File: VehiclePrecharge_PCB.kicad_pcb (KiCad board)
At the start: 4 copper layers, 75 x 90 mm, 12 parts, among them K1 2-1904058-5

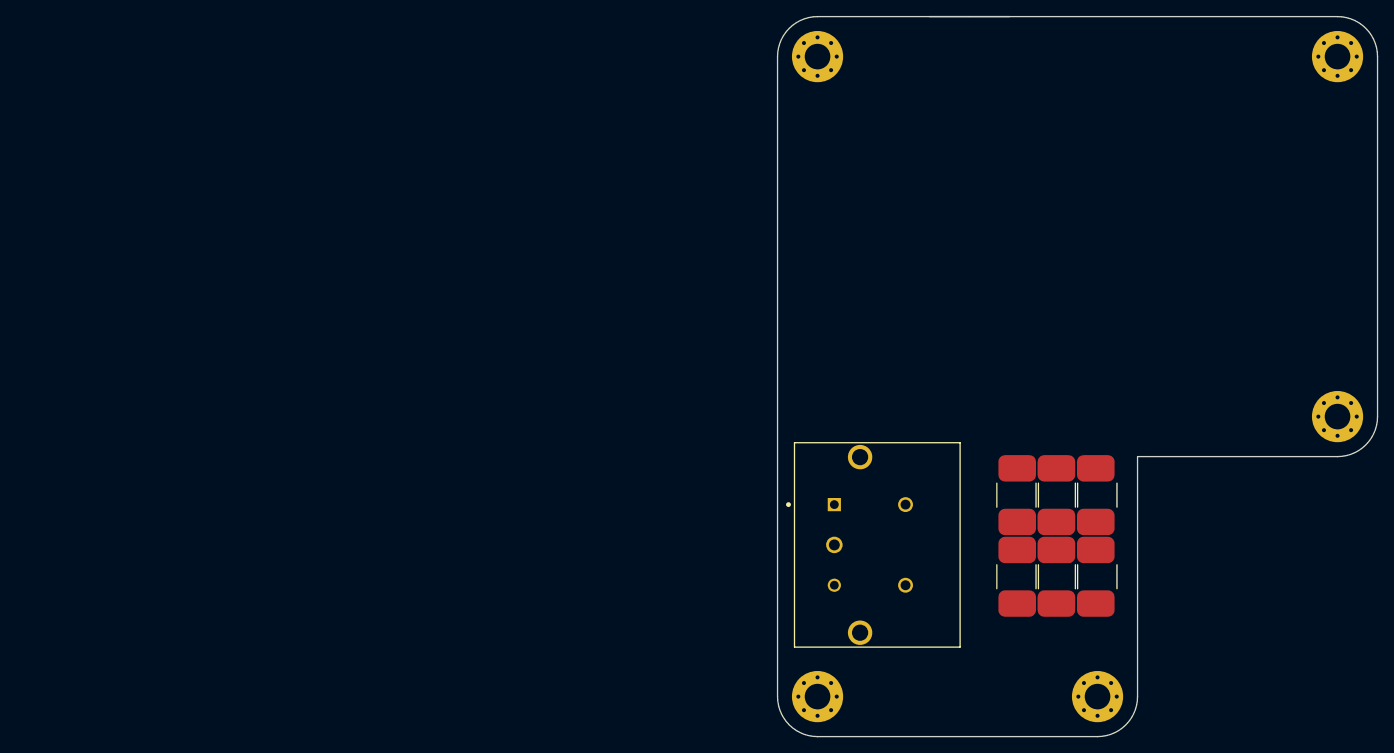
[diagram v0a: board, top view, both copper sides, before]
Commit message: Changed to DRV110A
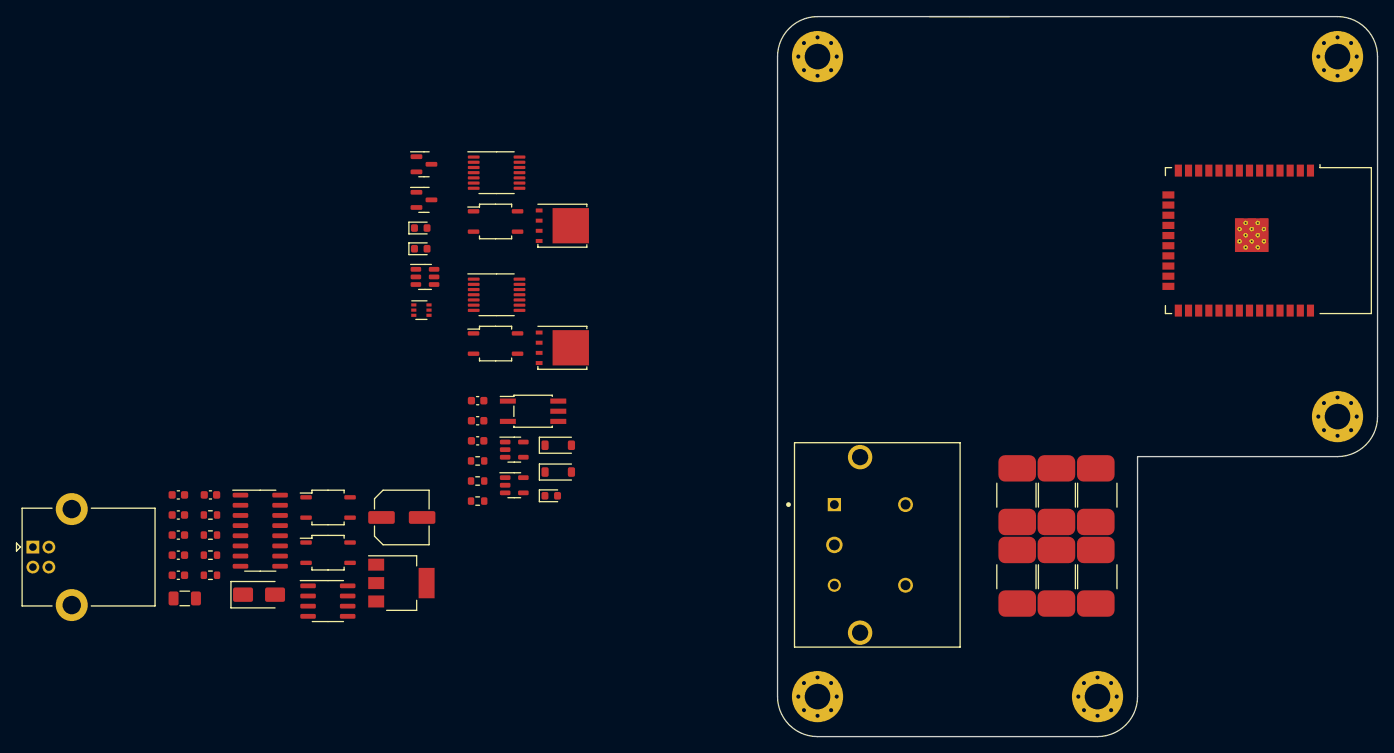
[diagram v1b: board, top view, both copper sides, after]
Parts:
- added C1: 100n, Capacitor_SMD:C_0603_1608Metric, F.Cu at (43.1, 114.8)
- added C10: 1u, Capacitor_SMD:C_0603_1608Metric, F.Cu at (47.1, 114.8)
- added C2: 100n, Capacitor_SMD:C_0603_1608Metric, F.Cu at (43.1, 117.3)
- added C3: 100n, Capacitor_SMD:C_0603_1608Metric, F.Cu at (43.1, 119.8)
- added C4: 22u, Capacitor_SMD:C_Elec_6.3x7.7, F.Cu at (71.0, 117.6)
- added C5: 0.1uF, Capacitor_SMD:C_0603_1608Metric, F.Cu at (43.1, 122.3)
- added C6: 100n, Capacitor_SMD:C_0603_1608Metric, F.Cu at (80.5, 103.0)
- added C7: 100n, Capacitor_SMD:C_0603_1608Metric, F.Cu at (80.5, 105.5)
- added C8: 100n, Capacitor_SMD:C_0603_1608Metric, F.Cu at (80.5, 108.0)
- added C9: 100n, Capacitor_SMD:C_0603_1608Metric, F.Cu at (43.1, 124.8)
- added D1: SS34, Diode_SMD:D_SMA, F.Cu at (53.2, 127.3)
- added D2: GREEN, LED_SMD:LED_0603_1608Metric, F.Cu at (73.4, 81.4)
- added D3: SM712_SOT23, Package_TO_SOT_SMD:SOT-23, F.Cu at (73.8, 73.5)
- added D4: 1N4148W, Diode_SMD:D_SOD-123, F.Cu at (90.6, 108.6)
- added D5: GREEN, LED_SMD:LED_0603_1608Metric, F.Cu at (73.4, 84.0)
- added D6: 1N4148W, Diode_SMD:D_SOD-123, F.Cu at (90.6, 111.9)
- added D7: Green, LED_SMD:LED_0603_1608Metric, F.Cu at (89.7, 114.9)
- added F1: 2A, Fuse:Fuse_1206_3216Metric, F.Cu at (43.9, 127.7)
- added J1: USB_B, Connector_USB:USB_B_Lumberg_2411_02_Horizontal, F.Cu at (24.9, 121.3)
- added Q1: BC847BS, Package_TO_SOT_SMD:SOT-363_SC-70-6, F.Cu at (73.5, 91.7)
- added Q2: SSM3J328R LF, Package_TO_SOT_SMD:SOT-23, F.Cu at (73.8, 77.9)
- added Q3: FDMS86255, Package_TO_SOT_SMD:TDSON-8-1, F.Cu at (91.1, 96.4)
- added Q4: FDMS86255, Package_TO_SOT_SMD:TDSON-8-1, F.Cu at (91.1, 81.1)
- added R11: 10k, Resistor_SMD:R_0603_1608Metric, F.Cu at (47.1, 119.8)
- added R13: 120, Resistor_SMD:R_0603_1608Metric, F.Cu at (47.1, 122.3)
- added R14: 2.2k, Resistor_SMD:R_0603_1608Metric, F.Cu at (47.1, 124.8)
- added R16: 1k, Resistor_SMD:R_0603_1608Metric, F.Cu at (80.5, 113.0)
- added R19: 1k, Resistor_SMD:R_0603_1608Metric, F.Cu at (80.5, 115.6)
- added R6: 10k, Resistor_SMD:R_0603_1608Metric, F.Cu at (80.5, 110.5)
- added R8: 10k, Resistor_SMD:R_0603_1608Metric, F.Cu at (47.1, 117.3)
- added U1: MCP9502PT-115E, Package_TO_SOT_SMD:SOT-23-5, F.Cu at (85.1, 109.1)
- added U10: MCP9502PT-115E, Package_TO_SOT_SMD:SOT-23-5, F.Cu at (85.1, 113.6)
- added U11: TLP2361, Package_SO:SO-5_4.4x3.6mm_P1.27mm, F.Cu at (87.4, 104.3)
- added U12: AQY212, Package_SO:SOP-4_3.8x4.1mm_P2.54mm, F.Cu at (61.8, 122.0)
- added U13: AQY212, Package_SO:SOP-4_3.8x4.1mm_P2.54mm, F.Cu at (82.8, 95.9)
- added U14: AQY212, Package_SO:SOP-4_3.8x4.1mm_P2.54mm, F.Cu at (82.8, 80.6)
- added U15: DRV110A, Package_SO:TSSOP-14_4.4x5mm_P0.65mm, F.Cu at (82.9, 89.8)
- added U16: DRV110A, Package_SO:TSSOP-14_4.4x5mm_P0.65mm, F.Cu at (82.9, 74.5)
- added U4: AQY212, Package_SO:SOP-4_3.8x4.1mm_P2.54mm, F.Cu at (61.8, 116.4)
- added U5: CH340C, Package_SO:SOIC-16_3.9x9.9mm_P1.27mm, F.Cu at (53.3, 119.3)
- added U6: ESP32-WROOM-32, RF_Module:ESP32-WROOM-32, F.Cu at (176.4, 83.0)
- added U7: USBLC6-2SC6, Package_TO_SOT_SMD:SOT-23-6, F.Cu at (73.9, 87.5)
- added U8: AMS1117-3.3, Package_TO_SOT_SMD:SOT-223-3_TabPin2, F.Cu at (71.0, 125.8)
- added U9: SN65HVD230, Package_SO:SOIC-8_3.9x4.9mm_P1.27mm, F.Cu at (61.8, 128.1)
- R10, R12: value 3k -> 10k
- R17, R18, R22: value 3k -> R_Small
- R9: value 3k -> 2.2k
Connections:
- K1 pad 1: (no net) -> Net-(K1-Pad1)
- K1 pad 2: (no net) -> GND
- K1 pad 4: (no net) -> unconnected-(K1-Pad4)
- K1 pad 5: (no net) -> unconnected-(K1-Pad5)
- K1 pad 7: (no net) -> unconnected-(K1-Pad7)
- R10 pad 1: (no net) -> Net-(Q1A-B1)
- R10 pad 2: (no net) -> DTR
- R12 pad 1: (no net) -> Net-(U9-Rs)
- R12 pad 2: (no net) -> GND
- R17 pad 1: (no net) -> Net-(R17-Pad1)
- R17 pad 2: (no net) -> GND
- R18 pad 1: (no net) -> Net-(U15-VIN)
- R18 pad 2: (no net) -> Net-(J6-Pin_1)
- R22 pad 1: (no net) -> Net-(U16-HOLD)
- R22 pad 2: (no net) -> GND
- R9 pad 1: (no net) -> GND
- R9 pad 2: (no net) -> Net-(D2-K)
